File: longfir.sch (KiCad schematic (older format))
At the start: 33 parts, among them J1 MJ-4PP-9, K1 diode-choc, K10 diode-choc, K11 diode-choc, K12 diode-choc, K13 diode-choc, K14 diode-choc, K15 diode-choc, K16 diode-choc, K17 diode-choc, K18 diode-choc, K19 diode-choc, K2 diode-choc, K20 diode-choc, K21 diode-choc, K22 diode-choc, K23 diode-choc, K24 diode-choc, K3 diode-choc, K4 diode-choc, K5 diode-choc, K6 diode-choc, K7 diode-choc, K8 diode-choc, K9 diode-choc, SW1 SW_PUSH, U1 ProMicro_r

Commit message: Fix switch footprint traces, Fix Tenting Puck
Footprints:
- Choc-diode traces as lines not custom pads, so show in gerber; diode silk end bar further from pad and mask
- Tenting Puck screws better clearance
- Move board label to lower center
- LEDs Ref# on fabrication layer, not silk
- Rewire TRRS to work with TRS cables

- TRRS moved in and up more
- Smoother curve on lower left edge cut

- Pads for haptic header
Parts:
- removed D1: SK6812-MINI-E, longfir:SK6812-MINI-E, symbol longfir:SK6812-MINI-E
- removed J1: MJ-4PP-9, kbd:MJ-4PP-9, symbol MMLid:MJ-4PP-9-kbd-corne-light-rescue
- added J1: MJ-4PP-9, kbd:MJ-4PP-9, symbol kbd:MJ-4PP-9
- added J2: Conn_01x05-Connector_Generic, mmccoyd:pimoroni_left_side_mount, symbol MMLid:Conn_01x05-Connector_Generic
- K1, K10, K11, K12, K13, K14, K15, K16, K17, K18, K19, K2, K20, K21, K22, K23, K24, K3, K4, K5, K6, K7, K8, K9: footprint longfir:pg1350-DR -> cridesgit:pg1350-DR
- renumbered D2 to D1, D3 to D2, D4 to D3, D5 to D4, D6 to D5
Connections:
- net labels added: SCL, SDA, trig
- net labels removed: col7
- wire segments 73 -> 80
- no-connect marks 6 -> 5
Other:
- note added: "TRRS plug enters jack from symbol bottom.\nJack contact labels:\nA: Sleeve (closest to cord on plug)\nD: Tip (furthest in)\nC: Ring 1 (closest to tip)\nB: Ring 2 (closest to sleeve on plug)"
- moved on the sheet: D1, D2, D3, D4, D5, K21, K22, K23, K24, SW1, U1

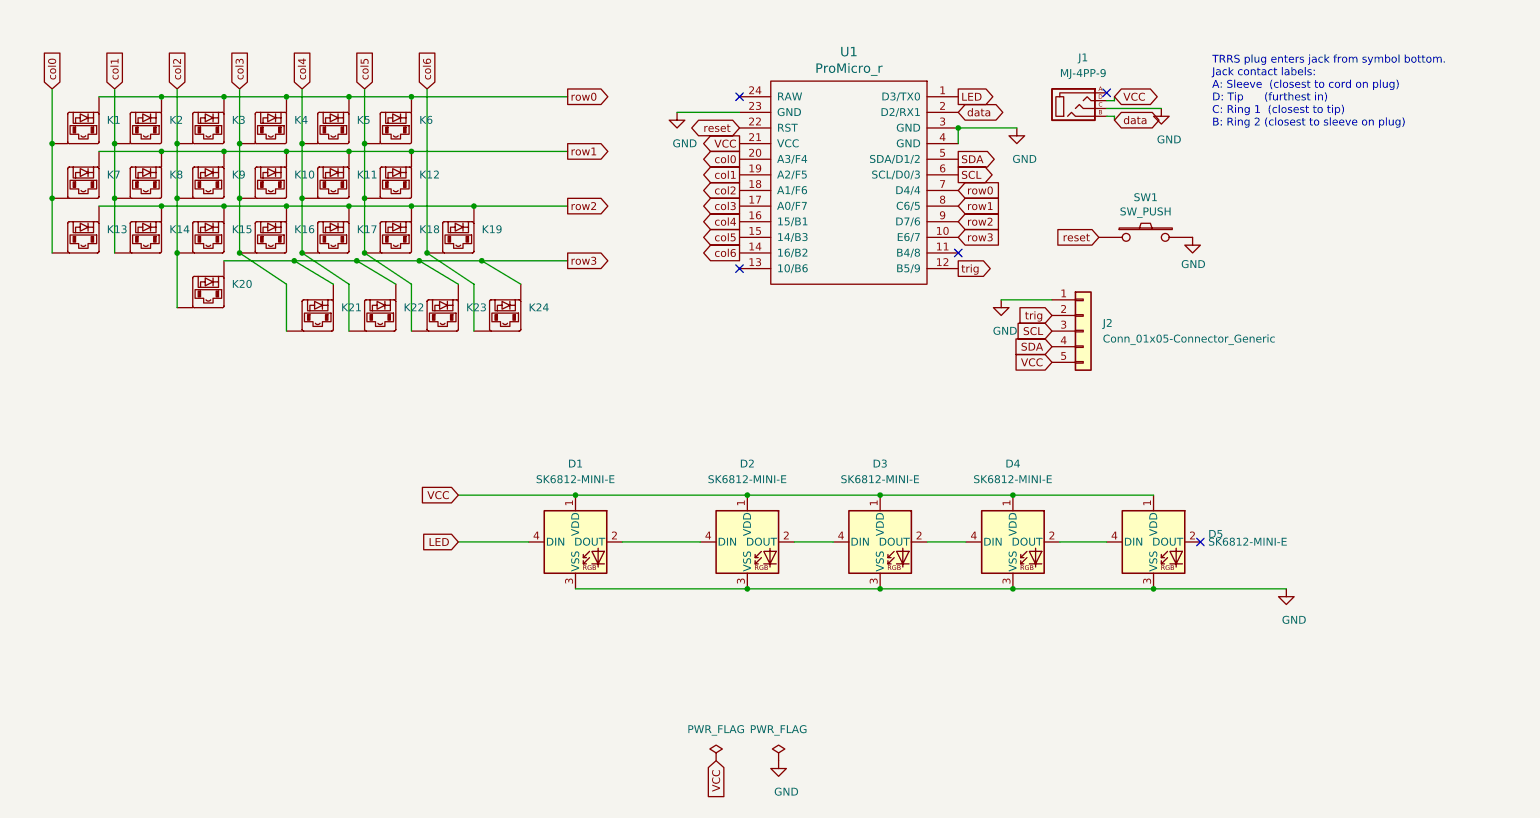
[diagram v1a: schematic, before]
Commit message: Use 6 columns. Bottom row traces run two cols over
- LEDs tucked under top edge of bottom row keys.
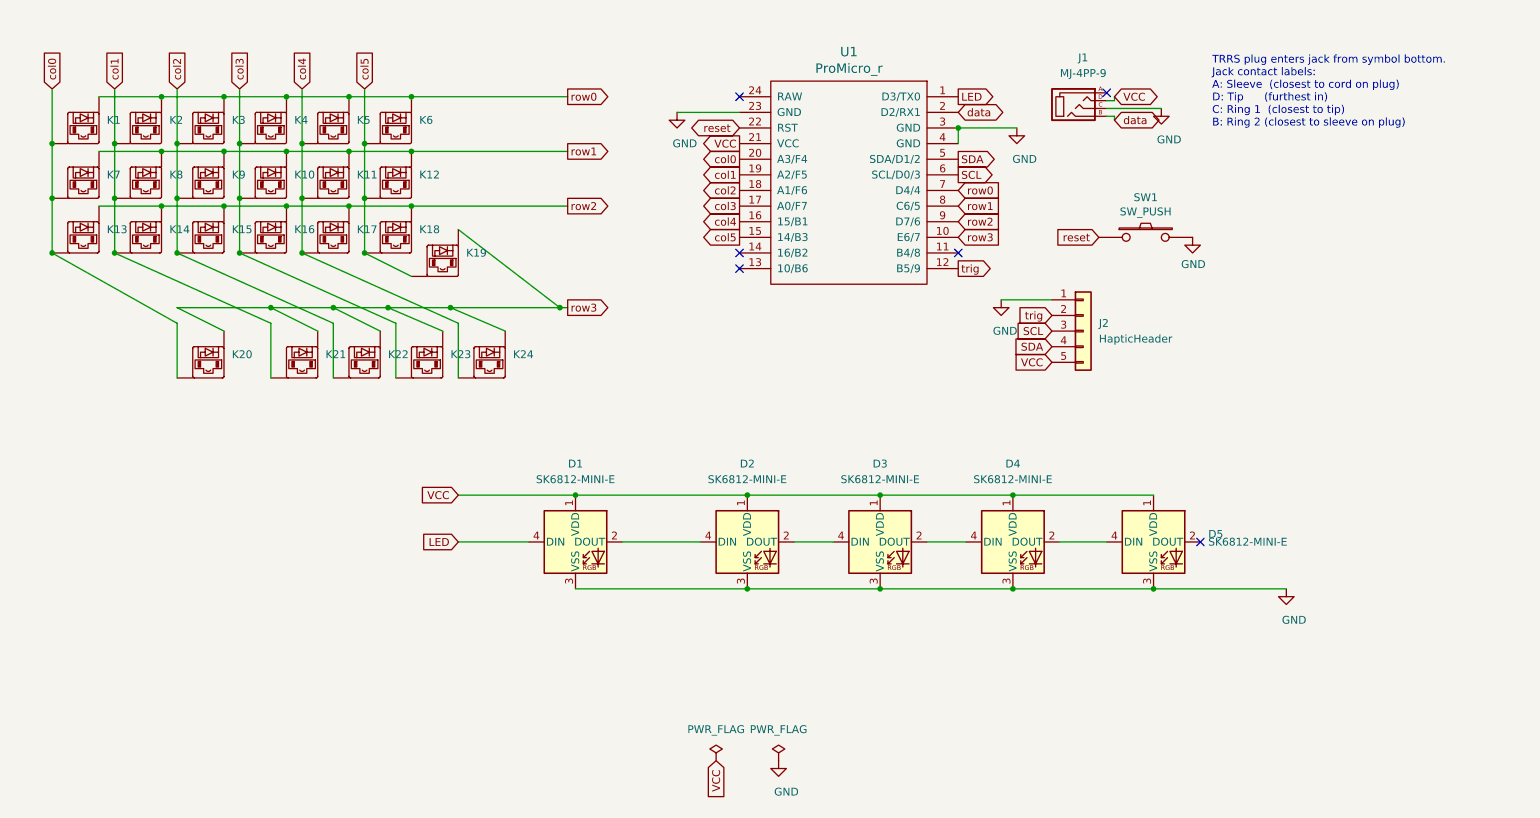
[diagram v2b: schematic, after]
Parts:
- J2: value Conn_01x05-Connector_Generic -> HapticHeader; footprint mmccoyd:pimoroni_left_side_mount -> longfir:HapticHeader_1x05
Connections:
- net col0: now also K20.1
- net col1: now also K21.1
- net col2: now also K22.1; no longer K20.1
- net col3: now also K23.1; no longer K21.1
- net col4: now also K24.1; no longer K22.1
- net col5: now also K19.1; no longer K23.1
- net row2: no longer K19.2
- net row3: now also K19.2
- removed net col6: K19.1, K24.1, U1.14 (16/B2)
- no-connect marks 5 -> 6
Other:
- moved on the sheet: K19, K20, K21, K22, K23, K24
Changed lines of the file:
@@
 $EndComp
-Wire Wire Line
-	1350 3850 1350 4200
 Wire Wire Line
 	1750 3850 1750 4200
@@
 Connection ~ 3650 3900
 $Comp
-L longfir:diode-choc K20
-U 1 1 619AC99A
-P 2350 4400
-F 0 "K20" H 2500 4400 50  0000 L CNN
-F 1 "diode-choc" H 2350 4150 50  0001 C CNN
-F 2 "cridesgit:pg1350-DR" H 2200 4400 50  0001 C CNN
-F 3 "" H 2200 4400 50  0001 C CNN
-	1    2350 4400
-	1    0    0    -1
-$EndComp
-$Comp
 L longfir:diode-choc K21
 U 1 1 619AD97C
-P 3050 4550
-F 0 "K21" H 3200 4550 50  0000 L CNN
-F 1 "diode-choc" H 3050 4300 50  0001 C CNN
-F 2 "cridesgit:pg1350-DR" H 2900 4550 50  0001 C CNN
-F 3 "" H 2900 4550 50  0001 C CNN
-	1    3050 4550
+P 2950 4850
+F 0 "K21" H 3100 4850 50  0000 L CNN
+F 1 "diode-choc" H 2950 4600 50  0001 C CNN
+F 2 "cridesgit:pg1350-DR" H 2800 4850 50  0001 C CNN
+F 3 "" H 2800 4850 50  0001 C CNN
+	1    2950 4850
 	1    0    0    -1
 $EndComp
@@
 L longfir:diode-choc K22
 U 1 1 619AEB0F
-P 3450 4550
-F 0 "K22" H 3600 4550 50  0000 L CNN
-F 1 "diode-choc" H 3450 4300 50  0001 C CNN
-F 2 "cridesgit:pg1350-DR" H 3300 4550 50  0001 C CNN
-F 3 "" H 3300 4550 50  0001 C CNN
-	1    3450 4550
+P 3350 4850
+F 0 "K22" H 3500 4850 50  0000 L CNN
+F 1 "diode-choc" H 3350 4600 50  0001 C CNN
+F 2 "cridesgit:pg1350-DR" H 3200 4850 50  0001 C CNN
+F 3 "" H 3200 4850 50  0001 C CNN
+	1    3350 4850
 	1    0    0    -1
 $EndComp
@@
 L longfir:diode-choc K23
 U 1 1 619B015D
-P 3850 4550
-F 0 "K23" H 4000 4550 50  0000 L CNN
-F 1 "diode-choc" H 3850 4300 50  0001 C CNN
-F 2 "cridesgit:pg1350-DR" H 3700 4550 50  0001 C CNN
-F 3 "" H 3700 4550 50  0001 C CNN
-	1    3850 4550
+P 3750 4850
+F 0 "K23" H 3900 4850 50  0000 L CNN
+F 1 "diode-choc" H 3750 4600 50  0001 C CNN
+F 2 "cridesgit:pg1350-DR" H 3600 4850 50  0001 C CNN
+F 3 "" H 3600 4850 50  0001 C CNN
+	1    3750 4850
 	1    0    0    -1
 $EndComp
@@
 L longfir:diode-choc K24
 U 1 1 619B142B
-P 4250 4550
-F 0 "K24" H 4400 4550 50  0000 L CNN
-F 1 "diode-choc" H 4250 4300 50  0001 C CNN
-F 2 "cridesgit:pg1350-DR" H 4100 4550 50  0001 C CNN
-F 3 "" H 4100 4550 50  0001 C CNN
-	1    4250 4550
+P 4150 4850
+F 0 "K24" H 4300 4850 50  0000 L CNN
+F 1 "diode-choc" H 4150 4600 50  0001 C CNN
+F 2 "cridesgit:pg1350-DR" H 4000 4850 50  0001 C CNN
+F 3 "" H 4000 4850 50  0001 C CNN
+	1    4150 4850
 	1    0    0    -1
 $EndComp
@@
 L longfir:diode-choc K19
 U 1 1 619B2C5C
-P 3950 4050
-F 0 "K19" H 4100 4050 50  0000 L CNN
-F 1 "diode-choc" H 3950 3800 50  0001 C CNN
-F 2 "cridesgit:pg1350-DR" H 3800 4050 50  0001 C CNN
-F 3 "" H 3800 4050 50  0001 C CNN
-	1    3950 4050
-	1    0    0    -1
-$EndComp
-Wire Wire Line
-	3650 3900 4050 3900
-Connection ~ 4050 3900
-Wire Wire Line
-	2150 4550 2150 4200
+P 3850 4200
+F 0 "K19" H 4000 4200 50  0000 L CNN
+F 1 "diode-choc" H 3850 3950 50  0001 C CNN
+F 2 "cridesgit:pg1350-DR" H 3700 4200 50  0001 C CNN
+F 3 "" H 3700 4200 50  0001 C CNN
+	1    3850 4200
+	1    0    0    -1
+$EndComp
 Connection ~ 2150 3850
 Wire Wire Line
 	2150 3850 2150 3500
-Connection ~ 2150 4200
 Wire Wire Line
 	2150 4200 2150 3850
@@
 Wire Wire Line
 	3350 4200 3350 3850
-Wire Wire Line
-	3750 4200 3750 3150
 $Comp
 L longfir:diode-choc K3
@@
 Text GLabel 3350 3150 1    50   Input ~ 0
 col5
-Text GLabel 3750 3150 1    50   Input ~ 0
-col6
-Text GLabel 4650 4250 2    50   Output ~ 0
+Text GLabel 4650 4550 2    50   Output ~ 0
 row3
 Text GLabel 4650 3900 2    50   Output ~ 0
 row2
-Wire Wire Line
-	3650 3550 4650 3550
 Wire Wire Line
 	3650 3200 4650 3200
@@
 Text GLabel 4650 3200 2    50   Output ~ 0
 row0
-Text GLabel 5750 4200 0    50   Output ~ 0
-col6
 Wire Wire Line
 	5350 3300 5750 3300
@@
 	1    0    0    -1
 $EndComp
-Wire Wire Line
-	4050 3900 4650 3900
 $Comp
 L pwr:PWR_FLAG #FLG02
@@
 	7800 6050 8100 6050
 NoConn ~ 5750 3200
-Wire Wire Line
-	2850 4700 2850 4400
-Wire Wire Line
-	3250 4700 3250 4400
-Wire Wire Line
-	3650 4700 3650 4400
-Wire Wire Line
-	4050 4700 4050 4400
-Wire Wire Line
-	4050 4400 3750 4200
-Connection ~ 3750 4200
-Wire Wire Line
-	3950 4400 3700 4250
-Connection ~ 3700 4250
-Wire Wire Line
-	3700 4250 4100 4250
-Wire Wire Line
-	4350 4400 4100 4250
-Connection ~ 4100 4250
-Wire Wire Line
-	4100 4250 4650 4250
-Wire Wire Line
-	2450 4250 2900 4250
-Wire Wire Line
-	3650 4400 3350 4200
-Connection ~ 3350 4200
-Wire Wire Line
-	3250 4400 2950 4200
-Connection ~ 2950 4200
-Wire Wire Line
-	2850 4400 2550 4200
-Connection ~ 2550 4200
-Wire Wire Line
-	3150 4400 2900 4250
-Connection ~ 2900 4250
-Wire Wire Line
-	2900 4250 3300 4250
-Wire Wire Line
-	3550 4400 3300 4250
-Connection ~ 3300 4250
-Wire Wire Line
-	3300 4250 3700 4250
 NoConn ~ 5750 4300
 Text GLabel 8150 3350 2    50   BiDi ~ 0
@@
 U 1 1 616B8147
 P 7950 4700
-F 0 "J2" H 8075 4750 50  0000 L CNN
-F 1 "Conn_01x05-Connector_Generic" H 8075 4650 50  0000 L CNN
-F 2 "mmccoyd:pimoroni_left_side_mount" H 7950 4700 50  0001 C CNN
+F 0 "J2" H 8050 4750 50  0000 L CNN
+F 1 "HapticHeader" H 8050 4650 50  0000 L CNN
+F 2 "longfir:HapticHeader_1x05" H 7950 4700 50  0001 C CNN
 F 3 "" H 7950 4700 50  0001 C CNN
 	1    7950 4700
@@
 Text GLabel 7150 4300 2    50   Output ~ 0
 trig
+Wire Wire Line
+	3650 3550 4650 3550
+Wire Wire Line
+	3650 3900 4650 3900
+Wire Wire Line
+	3950 4650 3950 5000
+Wire Wire Line
+	3850 4700 3500 4550
+Connection ~ 3500 4550
+Wire Wire Line
+	3500 4550 3900 4550
+Wire Wire Line
+	4250 4700 3900 4550
+Connection ~ 3900 4550
+Wire Wire Line
+	1350 3850 1350 4200
+Wire Wire Line
+	3550 4650 3550 5000
+Wire Wire Line
+	3150 4650 3150 5000
+Wire Wire Line
+	2750 4650 2750 5000
+$Comp
+L longfir:diode-choc K20
+U 1 1 619AC99A
+P 2350 4850
+F 0 "K20" H 2500 4850 50  0000 L CNN
+F 1 "diode-choc" H 2350 4600 50  0001 C CNN
+F 2 "cridesgit:pg1350-DR" H 2200 4850 50  0001 C CNN
+F 3 "" H 2200 4850 50  0001 C CNN
+	1    2350 4850
+	1    0    0    -1
+$EndComp
+Wire Wire Line
+	3450 4700 3150 4550
+Connection ~ 3150 4550
+Wire Wire Line
+	3150 4550 3500 4550
+Wire Wire Line
+	3050 4700 2750 4550
+Connection ~ 2750 4550
+Wire Wire Line
+	2750 4550 3150 4550
+NoConn ~ 5750 4200
+Wire Wire Line
+	3650 4350 3350 4200
+Connection ~ 3350 4200
+Wire Wire Line
+	3950 4650 2950 4200
+Connection ~ 2950 4200
+Wire Wire Line
+	3550 4650 2550 4200
+Connection ~ 2550 4200
+Wire Wire Line
+	3150 4650 2150 4200
+Connection ~ 2150 4200
+Wire Wire Line
+	2750 4650 1750 4200
+Connection ~ 1750 4200
+Wire Wire Line
+	2150 5000 2150 4650
+Wire Wire Line
+	2150 4650 1350 4200
+Connection ~ 1350 4200
+Wire Wire Line
+	3900 4550 4600 4550
+Wire Wire Line
+	3950 4050 4600 4550
+Connection ~ 4600 4550
+Wire Wire Line
+	4600 4550 4650 4550
+Wire Wire Line
+	2450 4700 2150 4550
+Wire Wire Line
+	2150 4550 2750 4550
 $EndSCHEMATC

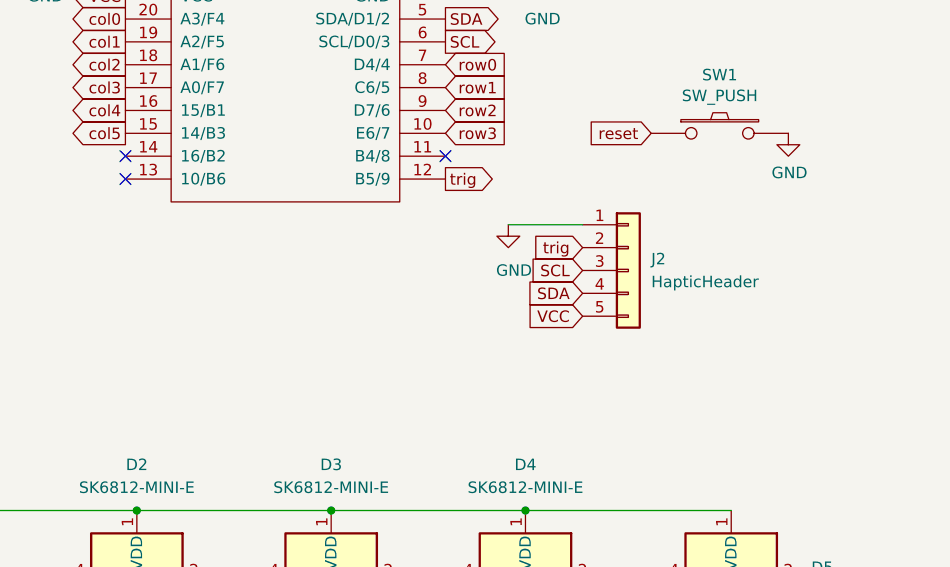
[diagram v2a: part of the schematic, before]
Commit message: Pull up resistors for I2C
- Use bottom plate as ground plate
- Sym Diode-Choc: suppress pin numbers in schematic
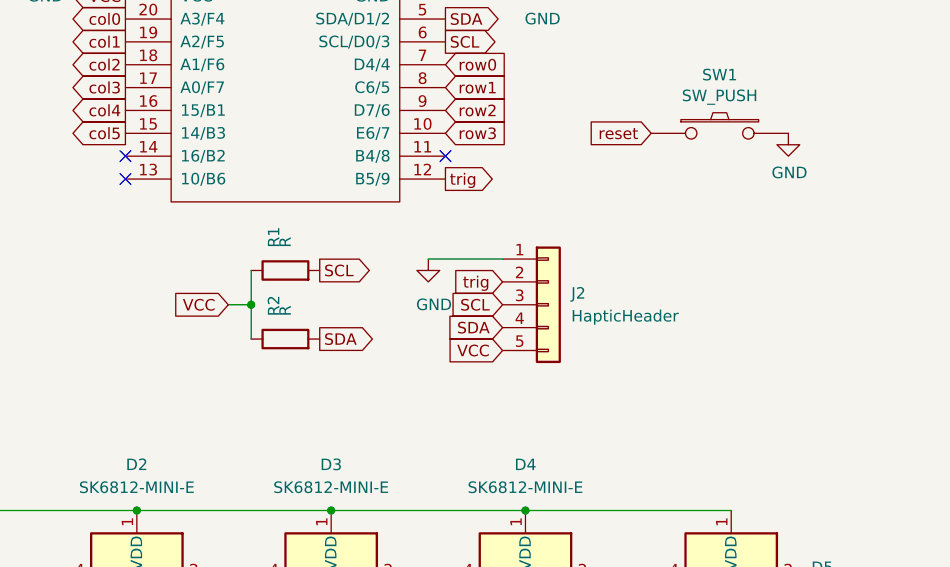
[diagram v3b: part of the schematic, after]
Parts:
- added R1, R2: R, ki_resist_smd:R_0805_2012Metric, symbol ki_device:R
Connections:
- net SCL: now also R1.2
- net SDA: now also R2.2
- net VCC: now also R1.1, R2.1
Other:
- moved on the sheet: J2
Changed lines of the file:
@@
 Sheet 1 1
 Title "LongFir Keyboard"
-Date ""
+Date "2021-09-10"
 Rev ""
-Comp ""
-Comment1 "A choc-spaced split keyboard with a layout between a Ferris and a Kyria"
+Comp "mmccoyd"
+Comment1 "A choc-spaced split keyboard with Ferris column stagger but more thumb and pinky keys."
 Comment2 ""
 Comment3 ""
@@
 L MMLid:Conn_01x05-Connector_Generic J2
 U 1 1 616B8147
-P 7950 4700
-F 0 "J2" H 8050 4750 50  0000 L CNN
-F 1 "HapticHeader" H 8050 4650 50  0000 L CNN
-F 2 "longfir:HapticHeader_1x05" H 7950 4700 50  0001 C CNN
-F 3 "" H 7950 4700 50  0001 C CNN
-	1    7950 4700
-	1    0    0    -1
-$EndComp
-Text GLabel 7750 4900 0    50   Input ~ 0
+P 7600 4850
+F 0 "J2" H 7700 4900 50  0000 L CNN
+F 1 "HapticHeader" H 7700 4800 50  0000 L CNN
+F 2 "longfir:HapticHeader_1x05" H 7600 4850 50  0001 C CNN
+F 3 "" H 7600 4850 50  0001 C CNN
+	1    7600 4850
+	1    0    0    -1
+$EndComp
+Text GLabel 7400 5050 0    50   Input ~ 0
 VCC
-Text GLabel 7750 4600 0    50   Input ~ 0
+Text GLabel 7400 4750 0    50   Input ~ 0
 trig
-Text GLabel 7750 4700 0    50   Input ~ 0
+Text GLabel 7400 4850 0    50   Input ~ 0
 SCL
-Text GLabel 7750 4800 0    50   Input ~ 0
+Text GLabel 7400 4950 0    50   Input ~ 0
 SDA
 $Comp
 L pwr:GND #PWR07
 U 1 1 616C872C
-P 7425 4500
-F 0 "#PWR07" H 7425 4250 50  0001 C CNN
-F 1 "GND" H 7450 4300 50  0000 C CNN
-F 2 "" H 7425 4500 50  0001 C CNN
-F 3 "" H 7425 4500 50  0001 C CNN
-	1    7425 4500
-	1    0    0    -1
-$EndComp
-Wire Wire Line
-	7425 4500 7750 4500
+P 7075 4650
+F 0 "#PWR07" H 7075 4400 50  0001 C CNN
+F 1 "GND" H 7100 4450 50  0000 C CNN
+F 2 "" H 7075 4650 50  0001 C CNN
+F 3 "" H 7075 4650 50  0001 C CNN
+	1    7075 4650
+	1    0    0    -1
+$EndComp
+Wire Wire Line
+	7075 4650 7400 4650
 Wire Wire Line
 	7150 3400 7525 3400
@@
 Wire Wire Line
 	2150 4550 2750 4550
+$Comp
+L ki_device:R R2
+U 1 1 618CD67C
+P 6450 5000
+F 0 "R2" H 6550 5050 50  0000 L CNN
+F 1 "R" H 6550 5000 50  0000 L CNN
+F 2 "ki_resist_smd:R_0805_2012Metric" V 6380 5000 50  0001 C CNN
+F 3 "~" H 6450 5000 50  0001 C CNN
+	1    6450 5000
+	0    -1   -1   0
+$EndComp
+Text GLabel 6600 4700 2    50   Output ~ 0
+SCL
+Text GLabel 6600 5000 2    50   Output ~ 0
+SDA
+$Comp
+L ki_device:R R1
+U 1 1 618CC9AE
+P 6450 4700
+F 0 "R1" H 6550 4750 50  0000 L CNN
+F 1 "R" H 6550 4700 50  0000 L CNN
+F 2 "ki_resist_smd:R_0805_2012Metric" V 6380 4700 50  0001 C CNN
+F 3 "~" H 6450 4700 50  0001 C CNN
+	1    6450 4700
+	0    -1   -1   0
+$EndComp
+Text GLabel 6200 4850 0    50   Input ~ 0
+VCC
+Wire Wire Line
+	6300 4700 6300 4850
+Wire Wire Line
+	6300 4850 6200 4850
+Connection ~ 6300 4850
+Wire Wire Line
+	6300 4850 6300 5000
 $EndSCHEMATC

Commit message: Scheme: Value and Reference cleanup
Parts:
- removed J1: MJ-4PP-9, kbd:MJ-4PP-9, symbol kbd:MJ-4PP-9
- added J2: TRRS, longfir:MJ-4PP-9, symbol longfir:TRRS
- J1: renamed from J2; value HapticHeader -> Haptic; footprint longfir:HapticHeader_1x05 -> longfir:PomoroniHaptic
- K1, K10, K11, K12, K13, K14, K15, K16, K17, K18, K19, K2, K20, K21, K22, K23, K24, K3, K4, K5, K6, K7, K8, K9: footprint cridesgit:pg1350-DR -> longfir:pg1350-DR
- R1: value R -> R:SCL; footprint ki_resist_smd:R_0805_2012Metric -> longfir:R_0805_2012Metric_DoubleSided
- R2: value R -> R:SDA; footprint ki_resist_smd:R_0805_2012Metric -> longfir:R_0805_2012Metric_DoubleSided
- SW1: value SW_PUSH -> Reset; footprint keebio:SW_Tactile_SPST_Angled_MJTP1117 -> longfir:SW_Tactile_SPST_Angled_MJTP1117
- U1: footprint kbd:ProMicro_v2 -> longfir:ProMicro_v2
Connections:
- net labels removed: trig
- wire segments 86 -> 85
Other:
- note removed: "TRRS plug enters jack from symbol bottom.\nJack contact labels:\nA: Sleeve (closest to cord on plug)\nD: Tip (furthest in)\nC: Ring 1 (closest to tip)\nB: Ring 2 (closest to sleeve on plug)"
- moved on the sheet: J1, K1, K10, K11, K12, K13, K14, K15, K16, K17, K18, K19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
